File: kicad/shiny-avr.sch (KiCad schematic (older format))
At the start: 39 parts, among them J1 USB_B_Micro, J2 SWD, U1 AMS1117-3.3, U2 STM32F103C6Tx, U3 ATtiny85-20PU, U4 ATtiny85-20PU, Y1 8 MHz

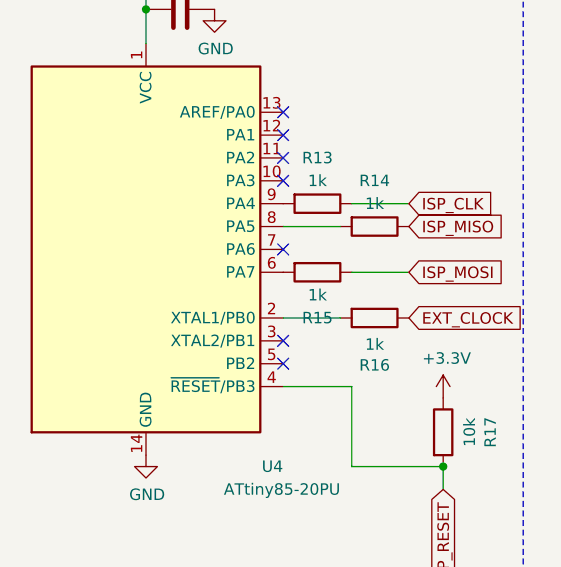
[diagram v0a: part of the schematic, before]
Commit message: fix: Swapped pins 6 and 7 on ATtinyX4 socket
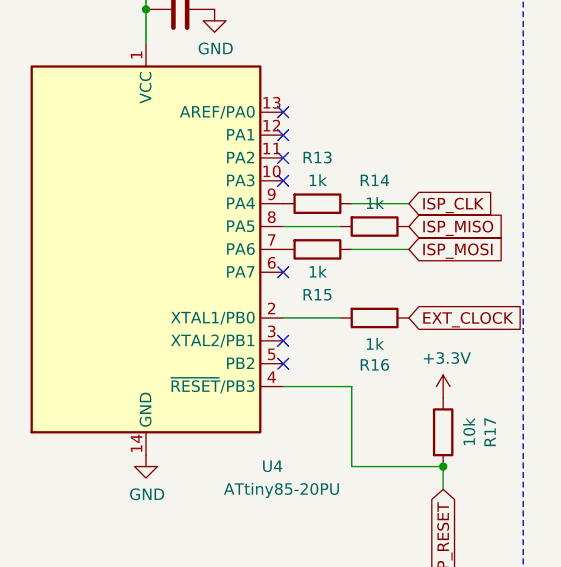
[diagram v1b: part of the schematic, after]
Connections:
- net at U4.6 (PA7): no longer R15.2
- net at U4.7 (PA6): now also R15.2
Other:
- moved on the sheet: R15
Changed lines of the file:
@@
 Text GLabel 10450 2150 2    50   Input ~ 0
 ISP_MISO
-Text GLabel 10450 2350 2    50   Input ~ 0
+Text GLabel 10450 2250 2    50   Input ~ 0
 ISP_MOSI
 Text GLabel 10600 3300 3    50   Input ~ 0
@@
 L Device:R R15
 U 1 1 6003EB14
-P 10050 2350
-F 0 "R15" V 10250 2350 50  0000 C CNN
-F 1 "1k" V 10150 2350 50  0000 C CNN
-F 2 "Resistor_SMD:R_0805_2012Metric_Pad1.20x1.40mm_HandSolder" V 9980 2350 50  0001 C CNN
-F 3 "~" H 10050 2350 50  0001 C CNN
-	1    10050 2350
+P 10050 2250
+F 0 "R15" V 10250 2250 50  0000 C CNN
+F 1 "1k" V 10150 2250 50  0000 C CNN
+F 2 "Resistor_SMD:R_0805_2012Metric_Pad1.20x1.40mm_HandSolder" V 9980 2250 50  0001 C CNN
+F 3 "~" H 10050 2250 50  0001 C CNN
+	1    10050 2250
 	0    1    1    0
 $EndComp
@@
 	10150 2150 9900 2150
 Wire Wire Line
-	10200 2350 10450 2350
-Wire Wire Line
 	10150 2550 9900 2550
 Wire Wire Line
@@
 NoConn ~ 9900 1850
 NoConn ~ 9900 1950
-NoConn ~ 9900 2250
+NoConn ~ 9900 2350
 NoConn ~ 9900 2750
+Wire Wire Line
+	10200 2250 10450 2250
 $EndSCHEMATC
